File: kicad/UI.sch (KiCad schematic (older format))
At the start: 15 parts, among them Q14 DMN3065LW-7, SW2 UPLOAD, U8 PCA9632

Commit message: フットプリントを改良
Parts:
- Q14: footprint TO_SOT_Packages_SMD:SOT-323_SC-70 -> Package_TO_SOT_SMD:SOT-323_SC-70
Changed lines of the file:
@@
 F 0 "Q14" H 7800 4450 50  0000 R CNN
 F 1 "DMN3065LW-7" H 7850 4150 50  0000 R CNN
-F 2 "TO_SOT_Packages_SMD:SOT-323_SC-70" H 8000 4400 50  0001 C CNN
+F 2 "Package_TO_SOT_SMD:SOT-323_SC-70" H 8000 4400 50  0001 C CNN
 F 3 "" H 7800 4300 50  0000 C CNN
 	1    7800 4300

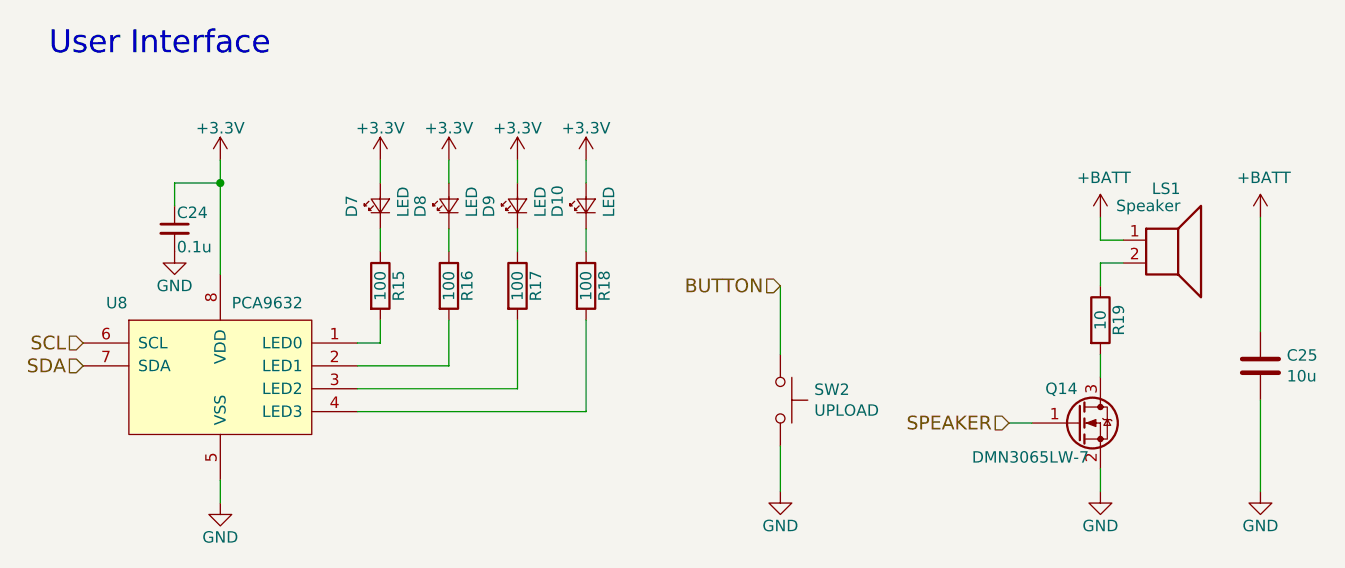
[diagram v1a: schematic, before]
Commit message: LEDの抵抗を集合抵抗に変更
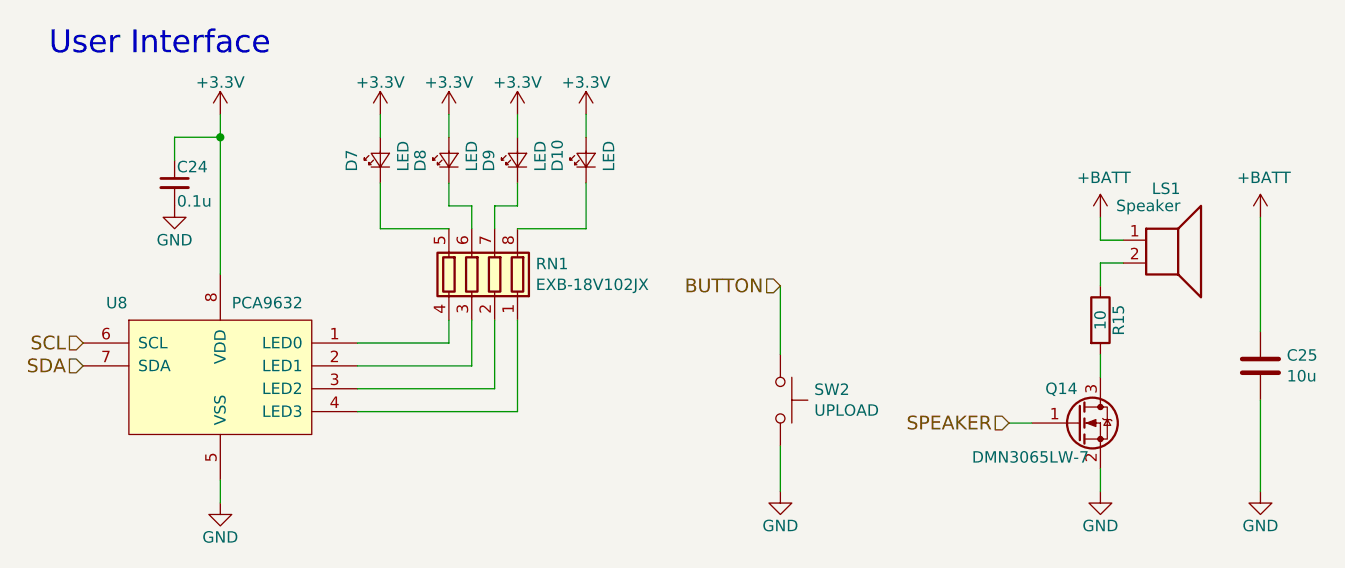
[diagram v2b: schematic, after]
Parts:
- removed R15, R16, R17, R18: 100, Resistor_SMD:R_0201_0603Metric, symbol Device:R
- added RN1: EXB-18V102JX, mouse:R_Array_Concave_4x0201, symbol Device:R_Pack04
- renumbered R19 to R15
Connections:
- net at D7.1 (K): now also RN1.5 (R4.2)
- net at U8.1 (LED0): now also RN1.4 (R4.1)
- net at D8.1 (K): now also RN1.6 (R3.2)
- net at U8.2 (LED1): now also RN1.3 (R3.1)
- net at D10.1 (K): now also RN1.8 (R1.2)
- net at U8.4 (LED3): now also RN1.1 (R1.1)
- net at D9.1 (K): now also RN1.7 (R2.2)
- net at U8.3 (LED2): now also RN1.2 (R2.1)
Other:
- moved on the sheet: C24, D10, D7, D8, D9
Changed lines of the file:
@@
 L power:+3.3V #PWR072
 U 1 1 5A202D5A
-P 4050 3150
-F 0 "#PWR072" H 4050 3000 50  0001 C CNN
-F 1 "+3.3V" H 4050 3290 50  0000 C CNN
-F 2 "" H 4050 3150 50  0001 C CNN
-F 3 "" H 4050 3150 50  0001 C CNN
-	1    4050 3150
-	1    0    0    -1
-$EndComp
-Wire Wire Line
-	4050 3150 4050 3250
+P 4050 2950
+F 0 "#PWR072" H 4050 2800 50  0001 C CNN
+F 1 "+3.3V" H 4050 3090 50  0000 C CNN
+F 2 "" H 4050 2950 50  0001 C CNN
+F 3 "" H 4050 2950 50  0001 C CNN
+	1    4050 2950
+	1    0    0    -1
+$EndComp
+Wire Wire Line
+	4050 2950 4050 3050
 $Comp
 L power:GND #PWR073
@@
 	4050 4650 4050 4550
 Wire Wire Line
-	5050 3250 5050 3150
-Wire Wire Line
-	5050 3450 5050 3550
+	5050 3050 5050 2950
 $Comp
 L power:+3.3V #PWR075
 U 1 1 5A204571
-P 5050 3150
-F 0 "#PWR075" H 5050 3000 50  0001 C CNN
-F 1 "+3.3V" H 5050 3290 50  0000 C CNN
-F 2 "" H 5050 3150 50  0001 C CNN
-F 3 "" H 5050 3150 50  0001 C CNN
-	1    5050 3150
-	1    0    0    -1
-$EndComp
-$Comp
-L Device:R R16
-U 1 1 5A20456B
-P 5050 3700
-F 0 "R16" V 5130 3700 50  0000 C CNN
-F 1 "100" V 5050 3700 50  0000 C CNN
-F 2 "Resistor_SMD:R_0201_0603Metric" V 4980 3700 50  0001 C CNN
-F 3 "" H 5050 3700 50  0001 C CNN
-	1    5050 3700
+P 5050 2950
+F 0 "#PWR075" H 5050 2800 50  0001 C CNN
+F 1 "+3.3V" H 5050 3090 50  0000 C CNN
+F 2 "" H 5050 2950 50  0001 C CNN
+F 3 "" H 5050 2950 50  0001 C CNN
+	1    5050 2950
 	1    0    0    -1
 $EndComp
@@
 L Device:LED_Small D8
 U 1 1 5A204565
-P 5050 3350
-F 0 "D8" H 5000 3475 50  0000 L CNN
-F 1 "LED" H 5000 3250 50  0000 L CNN
-F 2 "LED_SMD:LED_0402_1005Metric" V 5050 3350 50  0001 C CNN
-F 3 "" V 5050 3350 50  0001 C CNN
-	1    5050 3350
+P 5050 3150
+F 0 "D8" H 5000 3275 50  0000 L CNN
+F 1 "LED" H 5000 3050 50  0000 L CNN
+F 2 "LED_SMD:LED_0402_1005Metric" V 5050 3150 50  0001 C CNN
+F 3 "" V 5050 3150 50  0001 C CNN
+	1    5050 3150
 	0    -1   -1   0
 $EndComp
 Wire Wire Line
-	4750 3250 4750 3150
-Wire Wire Line
-	4750 3450 4750 3550
+	4750 3050 4750 2950
 $Comp
 L power:+3.3V #PWR074
 U 1 1 5A203D72
-P 4750 3150
-F 0 "#PWR074" H 4750 3000 50  0001 C CNN
-F 1 "+3.3V" H 4750 3290 50  0000 C CNN
-F 2 "" H 4750 3150 50  0001 C CNN
-F 3 "" H 4750 3150 50  0001 C CNN
-	1    4750 3150
-	1    0    0    -1
-$EndComp
-$Comp
-L Device:R R15
-U 1 1 5A1FD2AD
-P 4750 3700
-F 0 "R15" V 4830 3700 50  0000 C CNN
-F 1 "100" V 4750 3700 50  0000 C CNN
-F 2 "Resistor_SMD:R_0201_0603Metric" V 4680 3700 50  0001 C CNN
-F 3 "" H 4750 3700 50  0001 C CNN
-	1    4750 3700
+P 4750 2950
+F 0 "#PWR074" H 4750 2800 50  0001 C CNN
+F 1 "+3.3V" H 4750 3090 50  0000 C CNN
+F 2 "" H 4750 2950 50  0001 C CNN
+F 3 "" H 4750 2950 50  0001 C CNN
+	1    4750 2950
 	1    0    0    -1
 $EndComp
@@
 L Device:LED_Small D7
 U 1 1 5A203147
-P 4750 3350
-F 0 "D7" H 4700 3475 50  0000 L CNN
-F 1 "LED" H 4700 3250 50  0000 L CNN
-F 2 "LED_SMD:LED_0402_1005Metric" V 4750 3350 50  0001 C CNN
-F 3 "" V 4750 3350 50  0001 C CNN
-	1    4750 3350
+P 4750 3150
+F 0 "D7" H 4700 3275 50  0000 L CNN
+F 1 "LED" H 4700 3050 50  0000 L CNN
+F 2 "LED_SMD:LED_0402_1005Metric" V 4750 3150 50  0001 C CNN
+F 3 "" V 4750 3150 50  0001 C CNN
+	1    4750 3150
 	0    -1   -1   0
 $EndComp
 Wire Wire Line
-	5650 3250 5650 3150
-Wire Wire Line
-	5650 3450 5650 3550
+	5650 3050 5650 2950
 $Comp
 L power:+3.3V #PWR077
 U 1 1 5A20460C
-P 5650 3150
-F 0 "#PWR077" H 5650 3000 50  0001 C CNN
-F 1 "+3.3V" H 5650 3290 50  0000 C CNN
-F 2 "" H 5650 3150 50  0001 C CNN
-F 3 "" H 5650 3150 50  0001 C CNN
-	1    5650 3150
-	1    0    0    -1
-$EndComp
-$Comp
-L Device:R R18
-U 1 1 5A204612
-P 5650 3700
-F 0 "R18" V 5730 3700 50  0000 C CNN
-F 1 "100" V 5650 3700 50  0000 C CNN
-F 2 "Resistor_SMD:R_0201_0603Metric" V 5580 3700 50  0001 C CNN
-F 3 "" H 5650 3700 50  0001 C CNN
-	1    5650 3700
+P 5650 2950
+F 0 "#PWR077" H 5650 2800 50  0001 C CNN
+F 1 "+3.3V" H 5650 3090 50  0000 C CNN
+F 2 "" H 5650 2950 50  0001 C CNN
+F 3 "" H 5650 2950 50  0001 C CNN
+	1    5650 2950
 	1    0    0    -1
 $EndComp
@@
 L Device:LED_Small D10
 U 1 1 5A204618
-P 5650 3350
-F 0 "D10" H 5600 3475 50  0000 L CNN
-F 1 "LED" H 5600 3250 50  0000 L CNN
-F 2 "LED_SMD:LED_0402_1005Metric" V 5650 3350 50  0001 C CNN
-F 3 "" V 5650 3350 50  0001 C CNN
-	1    5650 3350
+P 5650 3150
+F 0 "D10" H 5600 3275 50  0000 L CNN
+F 1 "LED" H 5600 3050 50  0000 L CNN
+F 2 "LED_SMD:LED_0402_1005Metric" V 5650 3150 50  0001 C CNN
+F 3 "" V 5650 3150 50  0001 C CNN
+	1    5650 3150
 	0    -1   -1   0
 $EndComp
 Wire Wire Line
-	5350 3250 5350 3150
-Wire Wire Line
-	5350 3450 5350 3550
+	5350 3050 5350 2950
 $Comp
 L power:+3.3V #PWR076
 U 1 1 5A204620
-P 5350 3150
-F 0 "#PWR076" H 5350 3000 50  0001 C CNN
-F 1 "+3.3V" H 5350 3290 50  0000 C CNN
-F 2 "" H 5350 3150 50  0001 C CNN
-F 3 "" H 5350 3150 50  0001 C CNN
-	1    5350 3150
-	1    0    0    -1
-$EndComp
-$Comp
-L Device:R R17
-U 1 1 5A204626
-P 5350 3700
-F 0 "R17" V 5430 3700 50  0000 C CNN
-F 1 "100" V 5350 3700 50  0000 C CNN
-F 2 "Resistor_SMD:R_0201_0603Metric" V 5280 3700 50  0001 C CNN
-F 3 "" H 5350 3700 50  0001 C CNN
-	1    5350 3700
+P 5350 2950
+F 0 "#PWR076" H 5350 2800 50  0001 C CNN
+F 1 "+3.3V" H 5350 3090 50  0000 C CNN
+F 2 "" H 5350 2950 50  0001 C CNN
+F 3 "" H 5350 2950 50  0001 C CNN
+	1    5350 2950
 	1    0    0    -1
 $EndComp
@@
 L Device:LED_Small D9
 U 1 1 5A20462C
-P 5350 3350
-F 0 "D9" H 5300 3475 50  0000 L CNN
-F 1 "LED" H 5300 3250 50  0000 L CNN
-F 2 "LED_SMD:LED_0402_1005Metric" V 5350 3350 50  0001 C CNN
-F 3 "" V 5350 3350 50  0001 C CNN
-	1    5350 3350
+P 5350 3150
+F 0 "D9" H 5300 3275 50  0000 L CNN
+F 1 "LED" H 5300 3050 50  0000 L CNN
+F 2 "LED_SMD:LED_0402_1005Metric" V 5350 3150 50  0001 C CNN
+F 3 "" V 5350 3150 50  0001 C CNN
+	1    5350 3150
 	0    -1   -1   0
 $EndComp
-Wire Wire Line
-	4750 3850 4750 3950
-Wire Wire Line
-	4750 3950 4650 3950
-Wire Wire Line
-	4650 4050 5050 4050
-Wire Wire Line
-	5050 4050 5050 3850
-Wire Wire Line
-	4650 4150 5350 4150
-Wire Wire Line
-	5350 4150 5350 3850
-Wire Wire Line
-	4650 4250 5650 4250
-Wire Wire Line
-	5650 4250 5650 3850
 $Comp
 L Device:C_Small C24
 U 1 1 5A2A1F42
-P 3850 3450
-F 0 "C24" H 3860 3520 50  0000 L CNN
-F 1 "0.1u" H 3860 3370 50  0000 L CNN
-F 2 "Capacitor_SMD:C_0201_0603Metric" H 3850 3450 50  0001 C CNN
-F 3 "" H 3850 3450 50  0001 C CNN
-	1    3850 3450
+P 3850 3250
+F 0 "C24" H 3860 3320 50  0000 L CNN
+F 1 "0.1u" H 3860 3170 50  0000 L CNN
+F 2 "Capacitor_SMD:C_0201_0603Metric" H 3850 3250 50  0001 C CNN
+F 3 "" H 3850 3250 50  0001 C CNN
+	1    3850 3250
 	1    0    0    -1
 $EndComp
@@
 L power:GND #PWR071
 U 1 1 5A2A2041
-P 3850 3550
-F 0 "#PWR071" H 3850 3300 50  0001 C CNN
-F 1 "GND" H 3850 3400 50  0000 C CNN
-F 2 "" H 3850 3550 50  0001 C CNN
-F 3 "" H 3850 3550 50  0001 C CNN
-	1    3850 3550
-	1    0    0    -1
-$EndComp
-Wire Wire Line
-	3850 3350 3850 3250
-Wire Wire Line
-	3850 3250 4050 3250
-Connection ~ 4050 3250
+P 3850 3350
+F 0 "#PWR071" H 3850 3100 50  0001 C CNN
+F 1 "GND" H 3850 3200 50  0000 C CNN
+F 2 "" H 3850 3350 50  0001 C CNN
+F 3 "" H 3850 3350 50  0001 C CNN
+	1    3850 3350
+	1    0    0    -1
+$EndComp
+Wire Wire Line
+	3850 3150 3850 3050
+Wire Wire Line
+	3850 3050 4050 3050
+Connection ~ 4050 3050
 $Comp
 L KERISE:PCA9632 U8
@@
 	7500 4300 7600 4300
 $Comp
-L Device:R R19
+L Device:R R15
 U 1 1 5B6725CD
 P 7900 3850
-F 0 "R19" V 7980 3850 50  0000 C CNN
+F 0 "R15" V 7980 3850 50  0000 C CNN
 F 1 "10" V 7900 3850 50  0000 C CNN
 F 2 "Resistor_SMD:R_0201_0603Metric" V 7830 3850 50  0001 C CNN
@@
 Wire Wire Line
 	7900 4000 7900 4100
-Wire Wire Line
-	4050 3250 4050 3650
 $Comp
 L Switch:SW_Push SW2
@@
 Wire Wire Line
 	8600 3900 8600 3400
+$Comp
+L Device:R_Pack04 RN1
+U 1 1 5C3F6DA5
+P 5150 3650
+F 0 "RN1" H 4870 3696 50  0000 R CNN
+F 1 "EXB-18V102JX" H 4870 3605 50  0000 R CNN
+F 2 "mouse:R_Array_Concave_4x0201" V 5425 3650 50  0001 C CNN
+F 3 "~" H 5150 3650 50  0001 C CNN
+	1    5150 3650
+	-1   0    0    -1
+$EndComp
+Wire Wire Line
+	5050 3250 5050 3350
+Wire Wire Line
+	5050 3350 5150 3350
+Wire Wire Line
+	5150 3350 5150 3450
+Wire Wire Line
+	5250 3450 5250 3350
+Wire Wire Line
+	5250 3350 5350 3350
+Wire Wire Line
+	5350 3350 5350 3250
+Wire Wire Line
+	5650 3250 5650 3450
+Wire Wire Line
+	5050 3450 4750 3450
+Wire Wire Line
+	4750 3450 4750 3250
+Wire Wire Line
+	4650 4150 5250 4150
+Wire Wire Line
+	5250 4150 5250 3850
+Wire Wire Line
+	5350 3850 5350 4250
+Wire Wire Line
+	5350 4250 4650 4250
+Wire Wire Line
+	5150 4050 5150 3850
+Wire Wire Line
+	4650 4050 5150 4050
+Wire Wire Line
+	5050 3850 5050 3950
+Wire Wire Line
+	4650 3950 5050 3950
+Wire Wire Line
+	4050 3050 4050 3650
+Wire Wire Line
+	5350 3450 5650 3450
 $EndSCHEMATC
